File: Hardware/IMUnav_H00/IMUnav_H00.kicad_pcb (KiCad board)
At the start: 4 copper layers, 80 x 100 mm, 215 parts, among them J1 Conn_01x03_Pin, J2 Conn_01x03_Pin, J3 Conn_01x03_Pin, J4 Conn_01x03_Pin, J5 Conn_01x03_Pin, J6 Conn_01x03_Pin, J7 918-418K2023S40001, J8 SMA6252A2-3GT50G-50, J9 Micro_SD_Card_Det_Hirose_DM3AT, Q1 S8050, Q2 S8050, SW1 MT-102, SW2 SW_SPST, SW3 SW_SPST, SW4 SW_SPST, SW5 SW_SPST, U1 STM32F446VETx, U10 ESP32-C3-MINI-1, U11 MPU-6050, U12 LSM303AGR, U13 ADIS16505-2BMLZ, U14 ADIS16505-x/PCBZ, U15 XC6206P332MR, U16 NEO-M8U, U17 XT25F256BWSIGT, U18 OLED_I2C, U2 TVS0500DRV, U3 74LVC2G02, U4 BQ24075RGT, U5 USBLC6-2P6, U6 HT7533-1, U7 TPS62823DLC, U8 USB2514B-AEZC-TR, U9 CH340G, X1 SX5M24.000M20F30TNN, X2 SX5M24.000M20F30TNN

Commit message: PCB routing
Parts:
- removed J1: Conn_01x03_Pin, Connector_PinHeader_2.54mm:PinHeader_1x03_P2.54mm_Vertical
- removed SWD1: Conn_01x06_Pin, Connector_PinHeader_2.54mm:PinHeader_1x06_P2.54mm_Vertical
- added J10: Conn_ARM_JTAG_SWD_10, Connector_PinHeader_1.27mm:PinHeader_2x05_P1.27mm_Vertical, F.Cu at (63.8, 27.6)
- added RESET2: SW_SPST, Button_Switch_SMD:SW_SPST_TL3342, F.Cu at (35.6, 57.1)
- moved C23 181.1 mm to (77.0, 79.1)
- moved C19 173.7 mm to (73.8, 79.1), turned to 180 degrees
- moved C24 171.0 mm to (73.7, 68.3), turned to 180 degrees
- moved R33 160.7 mm to (74.7, 71.5)
- moved C32 160.1 mm to (72.3, 65.8), turned to -90 degrees
- moved C35 159.4 mm to (65.2, 66.3), turned to -90 degrees
- moved SW2 157.8 mm to (35.0, 98.1), turned to 90 degrees
- moved C33 157.6 mm to (70.6, 65.8), turned to -90 degrees
- moved TP3 150.5 mm to (77.1, 58.9)
- moved C65 150.3 mm to (54.6, -33.7)
- moved R59 150.3 mm to (54.6, -26.1)
- moved R63 150.3 mm to (58.6, -33.7)
- moved R73 150.3 mm to (62.6, -26.1)
- moved R77 150.3 mm to (66.7, -33.7)
- moved R80 150.3 mm to (66.7, -26.1)
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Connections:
- C16 pad 1: Net-(SW1-B) -> Net-(SW1-A)
- SW1 pad 1: +BATT -> Net-(SW1-A)
- SW1 pad 2: Net-(SW1-B) -> +BATT
- TP4 pad 1: Net-(SW1-B) -> Net-(SW1-A)
- U4 pad 10: Net-(SW1-B) -> Net-(SW1-A)
- U4 pad 11: Net-(SW1-B) -> Net-(SW1-A)
- U8 pad 1: /ESP32/ESP_D- -> /USB+Power/USB1_D-
- U8 pad 2: /ESP32/ESP_D+ -> /USB+Power/USB1_D+
- U8 pad 8: /USB+Power/USB4_D- -> /ESP32/ESP_D-
- U8 pad 9: /USB+Power/USB4_D+ -> /ESP32/ESP_D+
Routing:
- net GND: track 65.7 -> 128.3 mm, vias 66 -> 142
- net +3V3: track 26.1 -> 53.6 mm, vias 11 -> 22
- net Net-(BT1-+): track 29.2 -> 56.7 mm
- net ESP_RST: track 0.00 -> 22.4 mm
- net Net-(SW1-A): track 0.00 -> 21.1 mm, vias 0 -> 1
- net Net-(Q2-C): track 0.00 -> 21.0 mm
- net Net-(U7-FB): track 0.00 -> 17.8 mm, vias 0 -> 2
- net +BATT: track 0.00 -> 16.7 mm
- net Net-(C31-Pad1): track 0.00 -> 13.5 mm
- net +5V: track 32.9 -> 46.1 mm, vias 8 -> 9
- net Net-(Q1-E): track 0.00 -> 12.8 mm, vias 0 -> 2
- net PWR_OFF: track 0.00 -> 9.18 mm, vias 0 -> 1
- net /ESP32/ESP_D+: track 5.76 -> 12.9 mm
- net /ESP32/ESP_D-: track 6.16 -> 13.3 mm
- net Net-(U1-PH0): track 0.00 -> 6.83 mm
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- added copper zone on F.Cu, net +3V3
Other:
- board size 80 x 100 mm -> 100 x 100 mm

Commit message: PCB routing
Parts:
- moved R83 147.9 mm to (5.97, 50.7)
- moved R84 143.4 mm to (9.78, 50.7)
- moved C69 141.1 mm to (45.6, 81.2), turned to -90 degrees
- moved R85 138.9 mm to (13.6, 50.7)
- moved C70 137.4 mm to (48.4, 81.2), turned to -90 degrees
- moved C71 133.8 mm to (51.1, 81.2), turned to -90 degrees
- moved C68 131.6 mm to (47.4, 67.3), turned to 180 degrees
- moved C72 130.1 mm to (53.7, 81.2), turned to -90 degrees
- moved D6 129.3 mm to (5.97, 52.3)
- moved D7 124.7 mm to (9.78, 52.3)
- moved D8 120.1 mm to (13.6, 52.3)
- moved R3 90.0 mm to (35.9, 58.5)
- moved C9 86.3 mm to (35.9, 60.1), turned to 180 degrees
- moved R4 80.7 mm to (44.5, 41.5), turned to 135 degrees
- moved R53 8.56 mm to (10.0, 42.7), turned to 90 degrees
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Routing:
- net BUTTON4: track 0.00 -> 59.3 mm
- net BUTTON1: track 0.00 -> 53.9 mm
- net BUTTON3: track 0.00 -> 53.7 mm
- net BUTTON2: track 0.00 -> 52.0 mm
- net GND: track 128.3 -> 145.1 mm, vias 142 -> 146
- net +3V3: track 53.6 -> 69.9 mm, vias 22 -> 24
- net SWD_NRST: track 0.00 -> 14.8 mm
- net Net-(U13-SCLK): track 0.90 -> 6.83 mm
- net Net-(U13-SYNC): track 0.90 -> 6.36 mm
- net Net-(U13-DOUT): track 0.90 -> 6.27 mm
- net Net-(U13-DIN): track 0.90 -> 6.13 mm
- net Net-(U13-~{CS}): track 0.90 -> 3.74 mm
- net ADIS_~{RST}: track 0.90 -> 3.68 mm
- net Net-(U13-DR): track 0.90 -> 3.68 mm
- net Net-(U1-PH0): track 6.83 -> 8.65 mm
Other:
- board size 100 x 100 mm -> 100 x 100.1 mm

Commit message: PCB routing
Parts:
- added C54: 10u, Capacitor_SMD:C_0805_2012Metric, F.Cu at (69.0, 40.3)
- C37: footprint Capacitor_SMD:C_0603_1608Metric -> Capacitor_SMD:C_0805_2012Metric
- moved R14 169.7 mm to (67.7, 88.1)
- moved C15 166.3 mm to (61.8, 74.2)
- moved C14 164.6 mm to (58.0, 74.2)
- moved R20 158.4 mm to (58.0, 77.2), turned to 180 degrees
- moved R23 156.8 mm to (61.8, 77.2), turned to 180 degrees
- moved R21 155.9 mm to (58.0, 75.7)
- moved R24 154.4 mm to (61.8, 75.7)
- moved R13 144.4 mm to (19.6, 98.6)
- moved R31 131.8 mm to (20.3, 83.2)
- moved R9 122.0 mm to (12.4, 81.2)
- moved R11 117.5 mm to (15.6, 81.2)
- moved R46 102.0 mm to (19.4, 62.0), turned to 180 degrees
- moved G2 94.3 mm to (86.9, 9.14)
- moved R63 87.9 mm to (76.5, 52.4), turned to 90 degrees
- moved R59 80.7 mm to (73.2, 52.4), turned to 90 degrees
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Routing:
- net +5V: track 46.1 -> 225.7 mm, vias 9 -> 10
- net /GPS/GPS_BCKP_POWER: track 4.67 -> 168.5 mm, vias 0 -> 3
- net /GPS/GPS_D+: track 7.63 -> 163.0 mm, vias 0 -> 2
- net /GPS/GPS_D-: track 8.03 -> 162.5 mm, vias 0 -> 2
- net /USB+Power/USB3_D-: track 5.64 -> 131.5 mm, vias 0 -> 2
- net /USB+Power/USB3_D+: track 5.23 -> 130.2 mm, vias 0 -> 2
- net ADIS_~{RST}: track 3.68 -> 87.1 mm, vias 1 -> 4
- net +3V3: track 69.9 -> 153.2 mm, vias 24 -> 63
- net ESP_RX1: track 0.00 -> 81.6 mm, vias 0 -> 3
- net ESP_TX1: track 0.00 -> 80.7 mm, vias 0 -> 3
- net GND: track 145.1 -> 220.2 mm, vias 146 -> 191
- net ESP_CTS1: track 0.00 -> 73.9 mm, vias 0 -> 2
- net ESP_RST: track 22.2 -> 94.8 mm, vias 0 -> 2
- net ESP_RTS1: track 0.00 -> 71.5 mm, vias 0 -> 2
- net OLED_SCL: track 0.00 -> 66.0 mm, vias 0 -> 1
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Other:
- board size 100 x 100.1 mm -> 100 x 100 mm

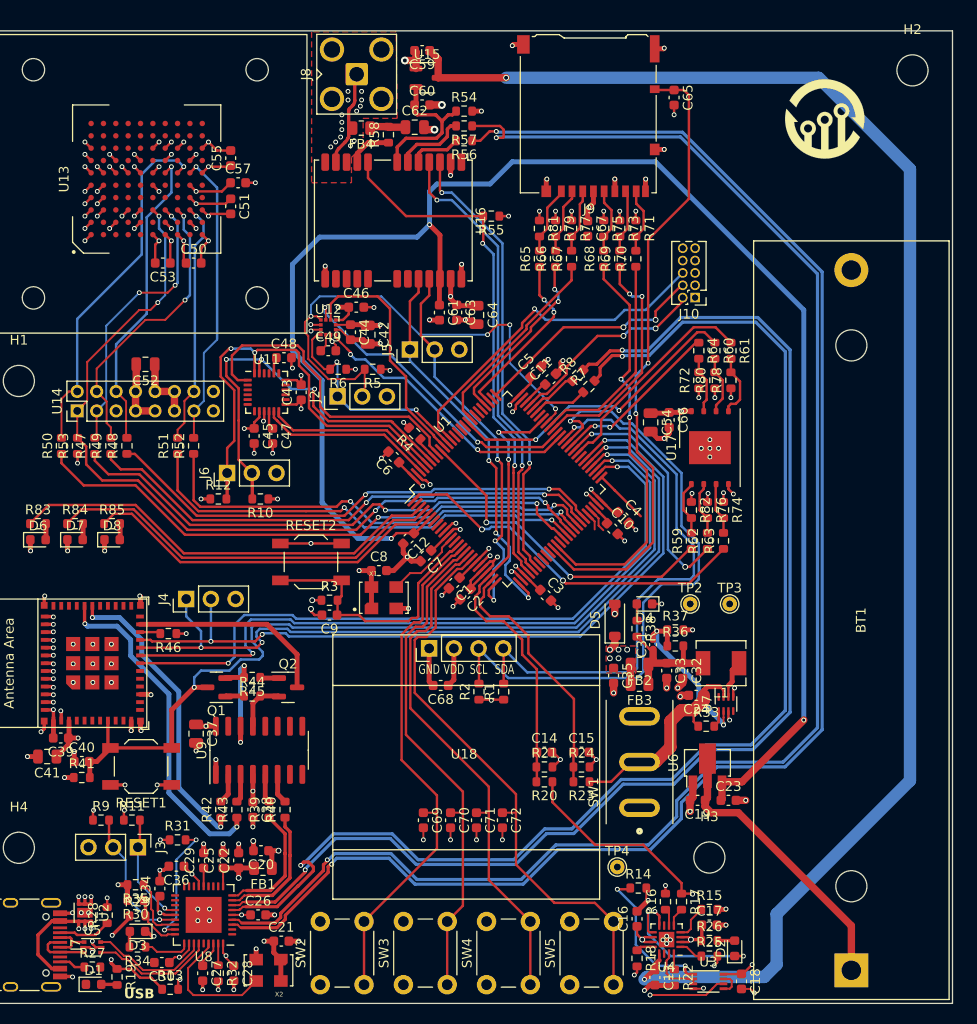
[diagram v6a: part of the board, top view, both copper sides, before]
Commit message: Semi-final PCB routing (copper only)
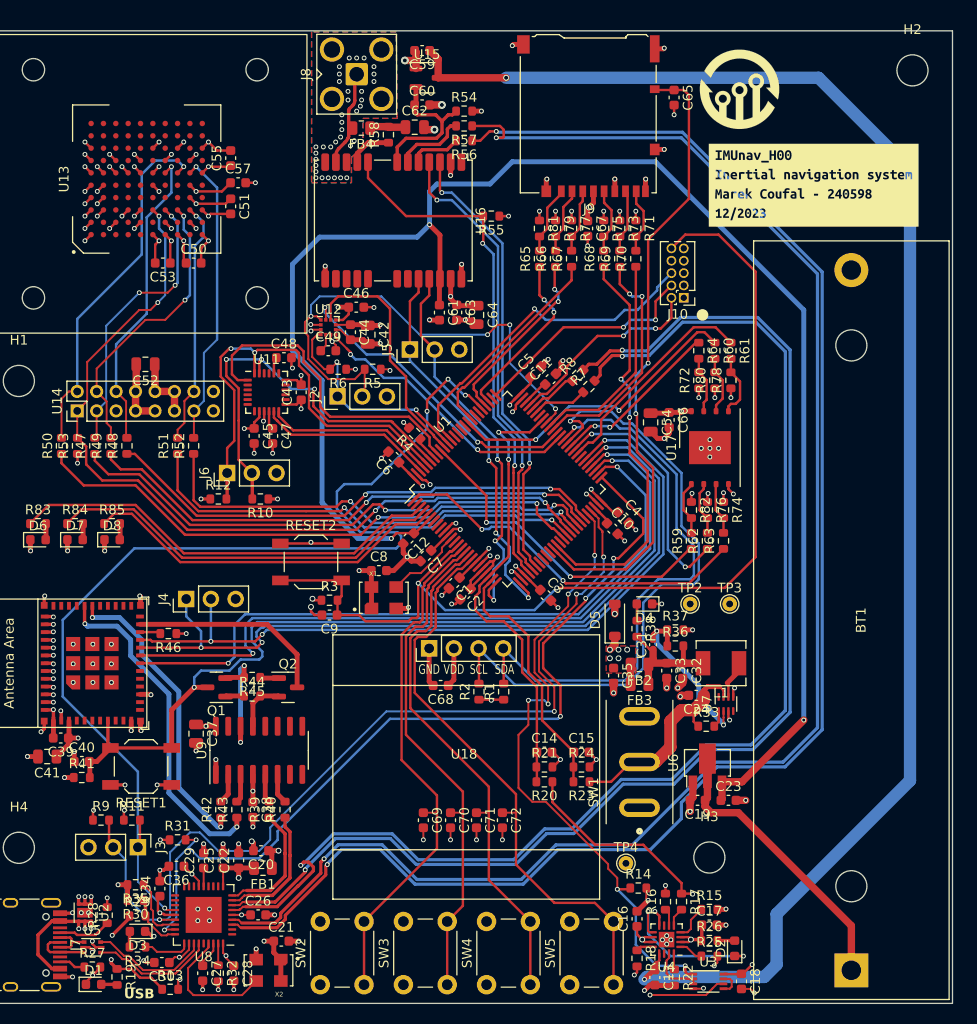
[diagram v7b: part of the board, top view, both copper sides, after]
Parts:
- added kibuzzard-656DA471: G***, kibuzzard-656DA471, F.Cu at (85.7, 15.9)
- moved G2 9.28 mm to (78.1, 6.10)
- moved J10 1.16 mm to (72.4, 27.4)
- moved TP4 0.97 mm to (66.4, 85.6)
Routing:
- net HUB_SDA: track 11.4 -> 109.1 mm, vias 1 -> 4
- net SWD_NRST: track 28.0 -> 106.3 mm, vias 0 -> 2
- net HUB_SCL: track 17.2 -> 95.2 mm, vias 1 -> 4
- net HUB_~{RESET}: track 18.5 -> 89.8 mm, vias 2 -> 5
- net PWR_OFF: track 17.3 -> 65.5 mm, vias 2 -> 6
- net GND: track 220.2 -> 225.2 mm, vias 191 -> 215
- net ESP_RTS1: track 71.5 -> 70.6 mm
- net /GPS/GPS_D-: track 162.5 -> 163.4 mm
- net SWD_SWO: track 35.8 -> 34.9 mm
- net unconnected-(U13-NC-PadG8): track 0.90 -> 0.00 mm, vias 1 -> 0
- net OLED_SDA: track 58.5 -> 59.2 mm
- net SWD_CLK: track 24.4 -> 23.8 mm
- net SD_CMD: track 20.7 -> 21.2 mm
- added copper zone on B.Cu, net GND
- added copper zone on In2.Cu, net GND

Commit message: Silkscreen layout
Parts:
- added G1: FEEC_logo, IMUnav:FEEC_logo, F.Cu at (82.3, 5.33)
- added G2: FEEC_logo_long, IMUnav:FEEC_logo_long, B.Cu at (43.4, 50.8)
- added TP5: TestPoint, TestPoint:TestPoint_THTPad_D1.5mm_Drill0.7mm, F.Cu at (76.7, 26.3)
- G4: renamed from G1; moved to B.Cu
- moved G4 77.3 mm to (55.5, 36.9), turned to 180 degrees
- moved G3 56.4 mm to (36.6, 44.2)
- moved kibuzzard-656DA471 2.71 mm to (83.1, 15.4)
- moved TP2 0.89 mm to (73.9, 58.9)
- renumbered C57 to C54, C59 to C56, C60 to C57, C61 to C58, C62 to C59, C63 to C60, C64 to C61, C65 to C62, C66 to C63, C54 to C64, C67 to C65, C68 to C66, C69 to C67, C70 to C68, C71 to C69, C72 to C70, G2 to G3, J10 to J1, RESET2 to RESET1, RESET1 to RESET2, TP4 to TP1
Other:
- board text added: "3V3"
- board text added: "CHRG"
- board text added: "USR1 USR2 USR3"
